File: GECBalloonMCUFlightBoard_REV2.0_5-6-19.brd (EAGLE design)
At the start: 160 x 100 mm, 74 parts, among them IC1 PIC32MX360F512L, Q1 IRF3704L-V, Q2 IRF3704L-V, U1 ADS1118, U2 ADS1118, X2 MALE_VGA, Y1 SG-636PCW_50.0000MC3__ROHS

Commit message: Added another ground pin to the DB15 connector and fixed the resistor layout to work with the temp sensors
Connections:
- net +3V3: now also R4.2
- net GND_3V3: now also X2.7; no longer R4.2
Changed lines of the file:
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@@
 <via x="138.43" y="94.45" extent="1-16" drill="0.9144" diameter="1.6002" shape="octagon"/>
 <via x="143.51" y="94.45" extent="1-16" drill="0.9144" diameter="1.6002" shape="octagon"/>
+<contactref element="R4" pad="2"/>
 </signal>
 <signal name="GND_3V3" class="1">
@@
 <wire x1="84.521" y1="35.846" x2="84.521" y2="32.919" width="0.4064" layer="1"/>
 <via x="84.521" y="32.919" extent="1-16" drill="0.3302" shape="octagon"/>
-<contactref element="R4" pad="2"/>
 <contactref element="X2" pad="8"/>
 <contactref element="Y1" pad="2"/>
@@
 <via x="135.89" y="86.83" extent="1-16" drill="0.9144" diameter="1.6002" shape="octagon"/>
 <via x="133.35" y="86.83" extent="1-16" drill="0.9144" diameter="1.6002" shape="octagon"/>
+<contactref element="X2" pad="7"/>
 </signal>
 <signal name="+3V3_PIC_ANALOG">

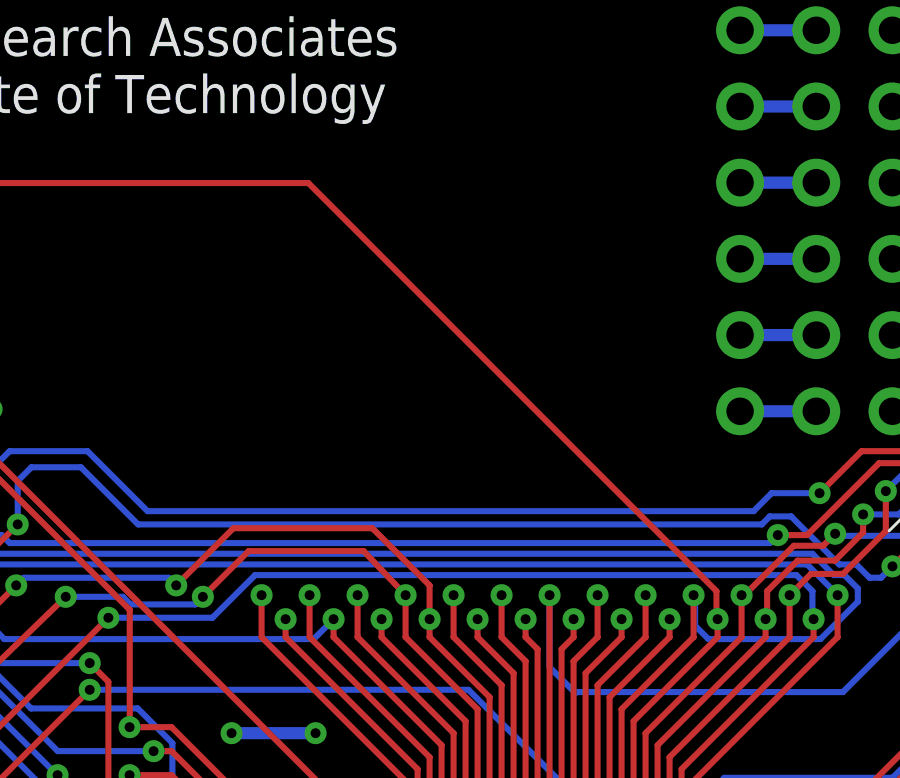
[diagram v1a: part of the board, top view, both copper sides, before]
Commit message: Added onboard I2C pullup resistors
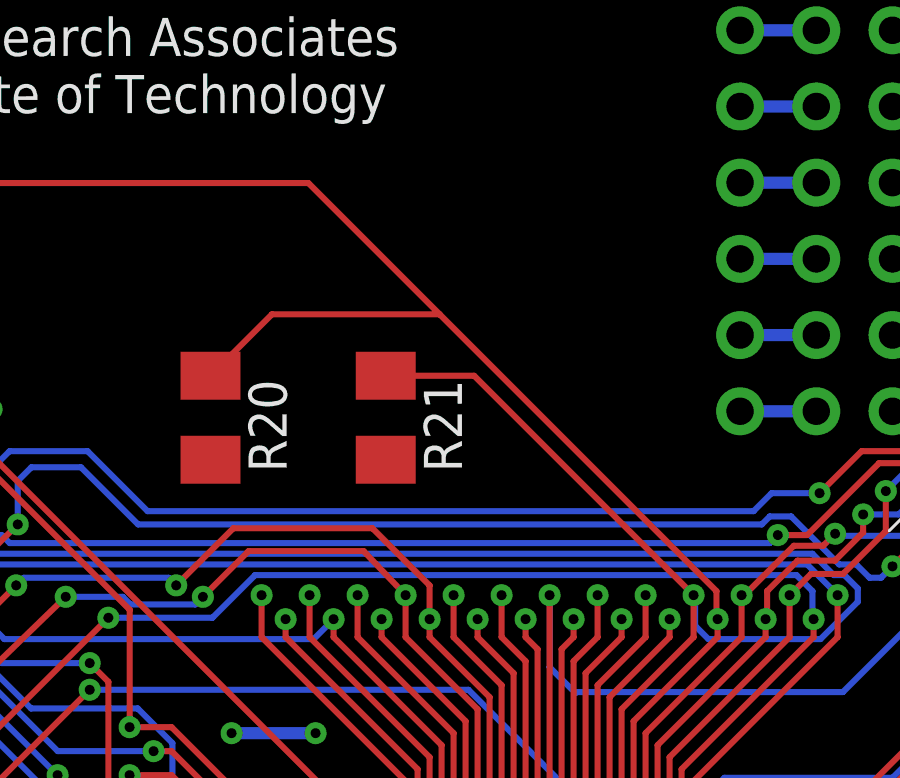
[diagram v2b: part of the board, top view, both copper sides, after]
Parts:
- added R20, R21: 10k, rcl:M1206
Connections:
- net +3V3: now also R20.2, R21.2
- net I2C_SCL: now also R21.1
- net I2C_SDA: now also R20.1
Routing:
- net I2C_SCL: track 81.3 -> 94.6 mm
- net I2C_SDA: track 98.6 -> 107.1 mm
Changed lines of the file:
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@@
 <element name="R18" library="resistor" package="R1206" value="680" x="94.996" y="59.563" rot="MR90"/>
 <element name="R19" library="resistor" package="R1206" value="510" x="100.584" y="59.563" rot="MR90"/>
+<element name="R20" library="rcl" package="M1206" value="10k" x="39.497" y="73.914" rot="R270"/>
+<element name="R21" library="rcl" package="M1206" value="10k" x="45.339" y="73.914" rot="R270"/>
 </elements>
 <signals>
@@
 <via x="143.51" y="94.45" extent="1-16" drill="0.9144" diameter="1.6002" shape="octagon"/>
 <contactref element="R4" pad="2"/>
+<contactref element="R20" pad="2"/>
+<contactref element="R21" pad="2"/>
 </signal>
 <signal name="GND_3V3" class="1">
@@
 <wire x1="55.6514" y1="67.9578" x2="55.6" y2="68" width="0.2032" layer="16"/>
 <via x="30.9372" y="69.6469" extent="1-16" drill="0.3302"/>
+<contactref element="R21" pad="1"/>
+<wire x1="55.6" y1="68" x2="48.286" y2="75.314" width="0.2032" layer="1"/>
+<wire x1="48.286" y1="75.314" x2="45.339" y2="75.314" width="0.2032" layer="1"/>
 </signal>
 <signal name="I2C_SDA">
@@
 <wire x1="13.5128" y1="81.7373" x2="12.9794" y2="81.2039" width="0.2032" layer="1"/>
 <wire x1="42.7609" y1="81.7373" x2="13.5128" y2="81.7373" width="0.2032" layer="1"/>
-<wire x1="56.3626" y1="68.1356" x2="42.7609" y2="81.7373" width="0.2032" layer="1"/>
+<wire x1="56.3626" y1="68.1356" x2="47.1361" y2="77.3621" width="0.2032" layer="1"/>
+<wire x1="47.1361" y1="77.3621" x2="42.7609" y2="81.7373" width="0.2032" layer="1"/>
 <wire x1="56.3626" y1="67.2466" x2="56.3626" y2="68.1356" width="0.2032" layer="1"/>
 <wire x1="8.89" y1="42.9769" x2="8.96" y2="42.971" width="0.2032" layer="1"/>
 <wire x1="56.3626" y1="67.2466" x2="56.4" y2="67.2" width="0.2032" layer="1"/>
+<contactref element="R20" pad="1"/>
+<wire x1="39.497" y1="75.314" x2="41.5451" y2="77.3621" width="0.2032" layer="1"/>
+<wire x1="41.5451" y1="77.3621" x2="47.1361" y2="77.3621" width="0.2032" layer="1"/>
 </signal>
 <signal name="CONDUCTIVITY_ENABLE">
